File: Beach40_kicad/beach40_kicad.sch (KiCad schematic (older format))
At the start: 75 parts, among them K1 RELAY_2RT, P1 LO In, P2 Mic In, P3 Audio Out, P4 ANT, Q1 BC548, Q2 2N2222, Q3 BD139, Q4 BD139, U1 LM386

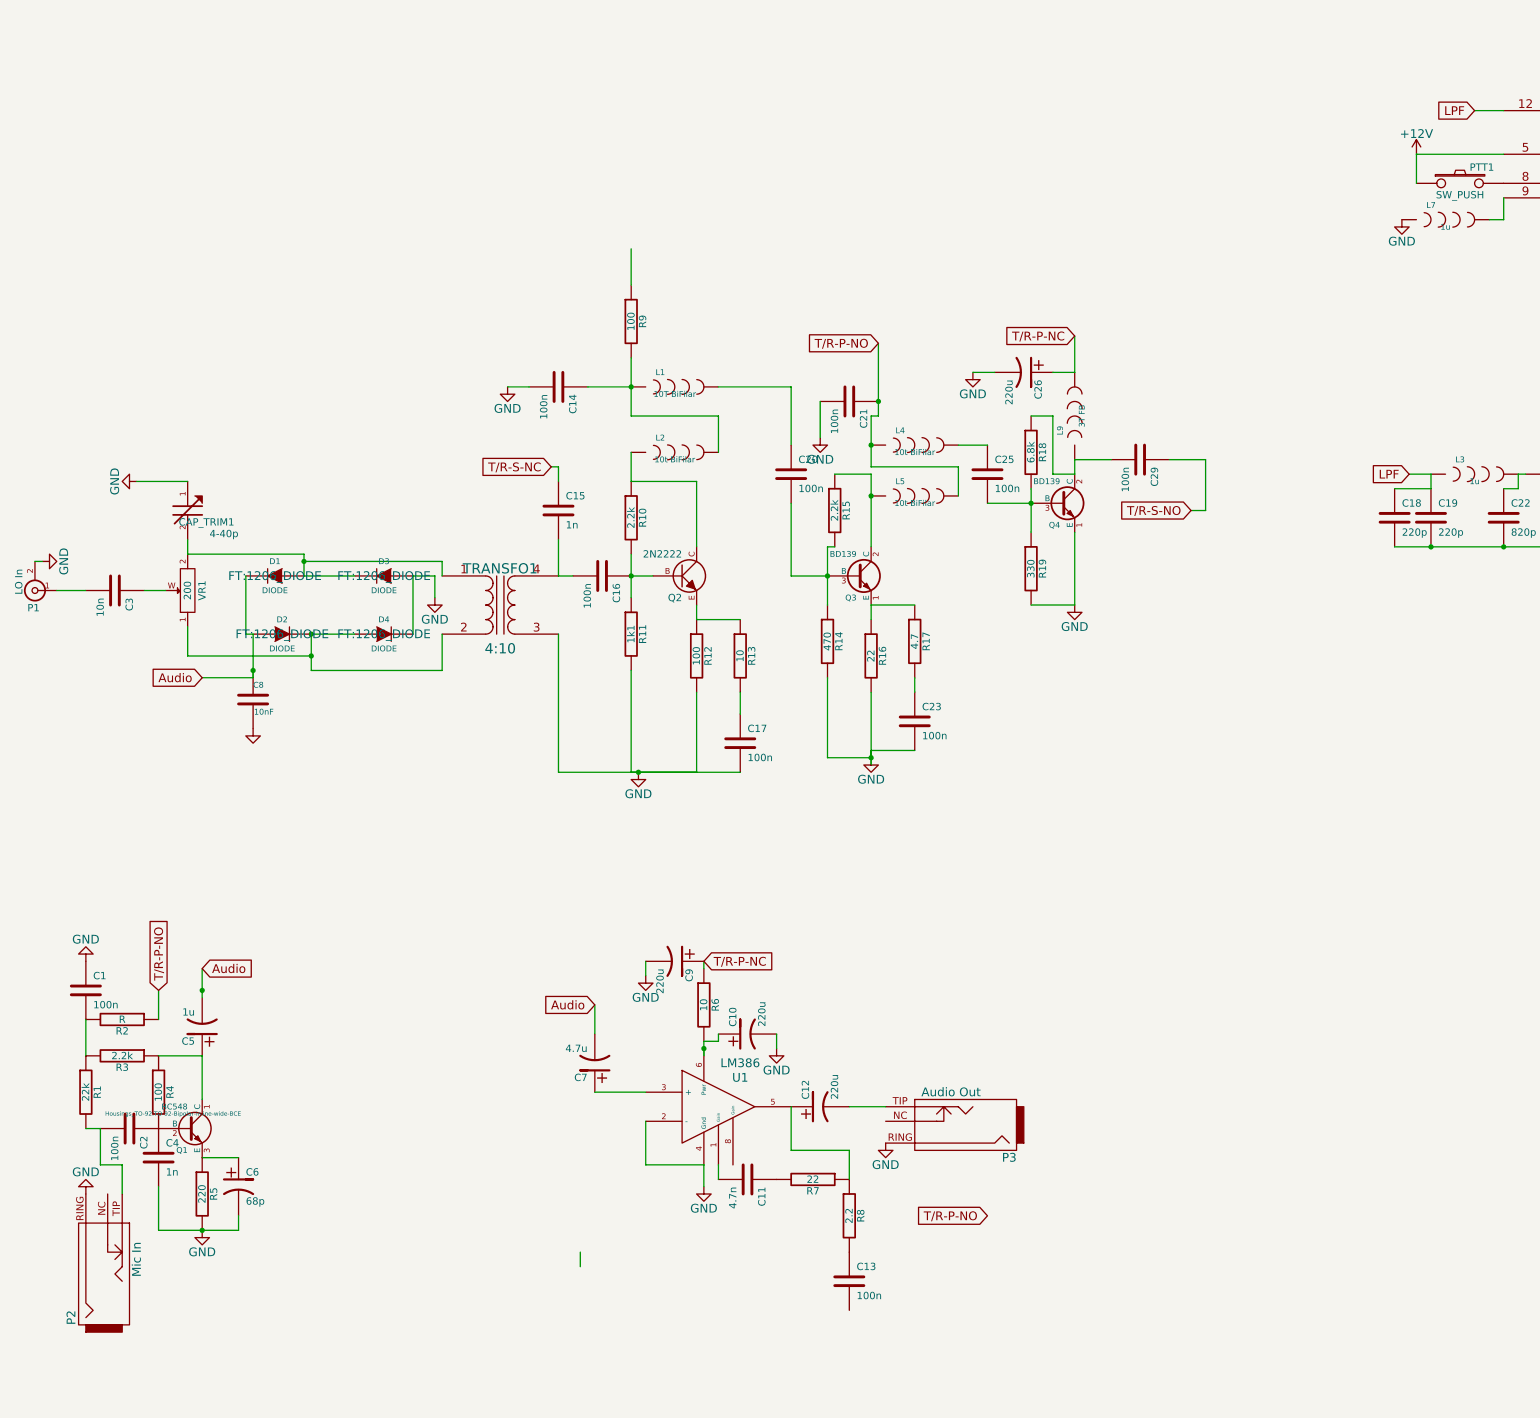
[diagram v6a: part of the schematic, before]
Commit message: Updated schematic to include shunt RC on LM386, Minor changes for ERC, still not quite right, damn gnds and +12v don't want to join the nets.
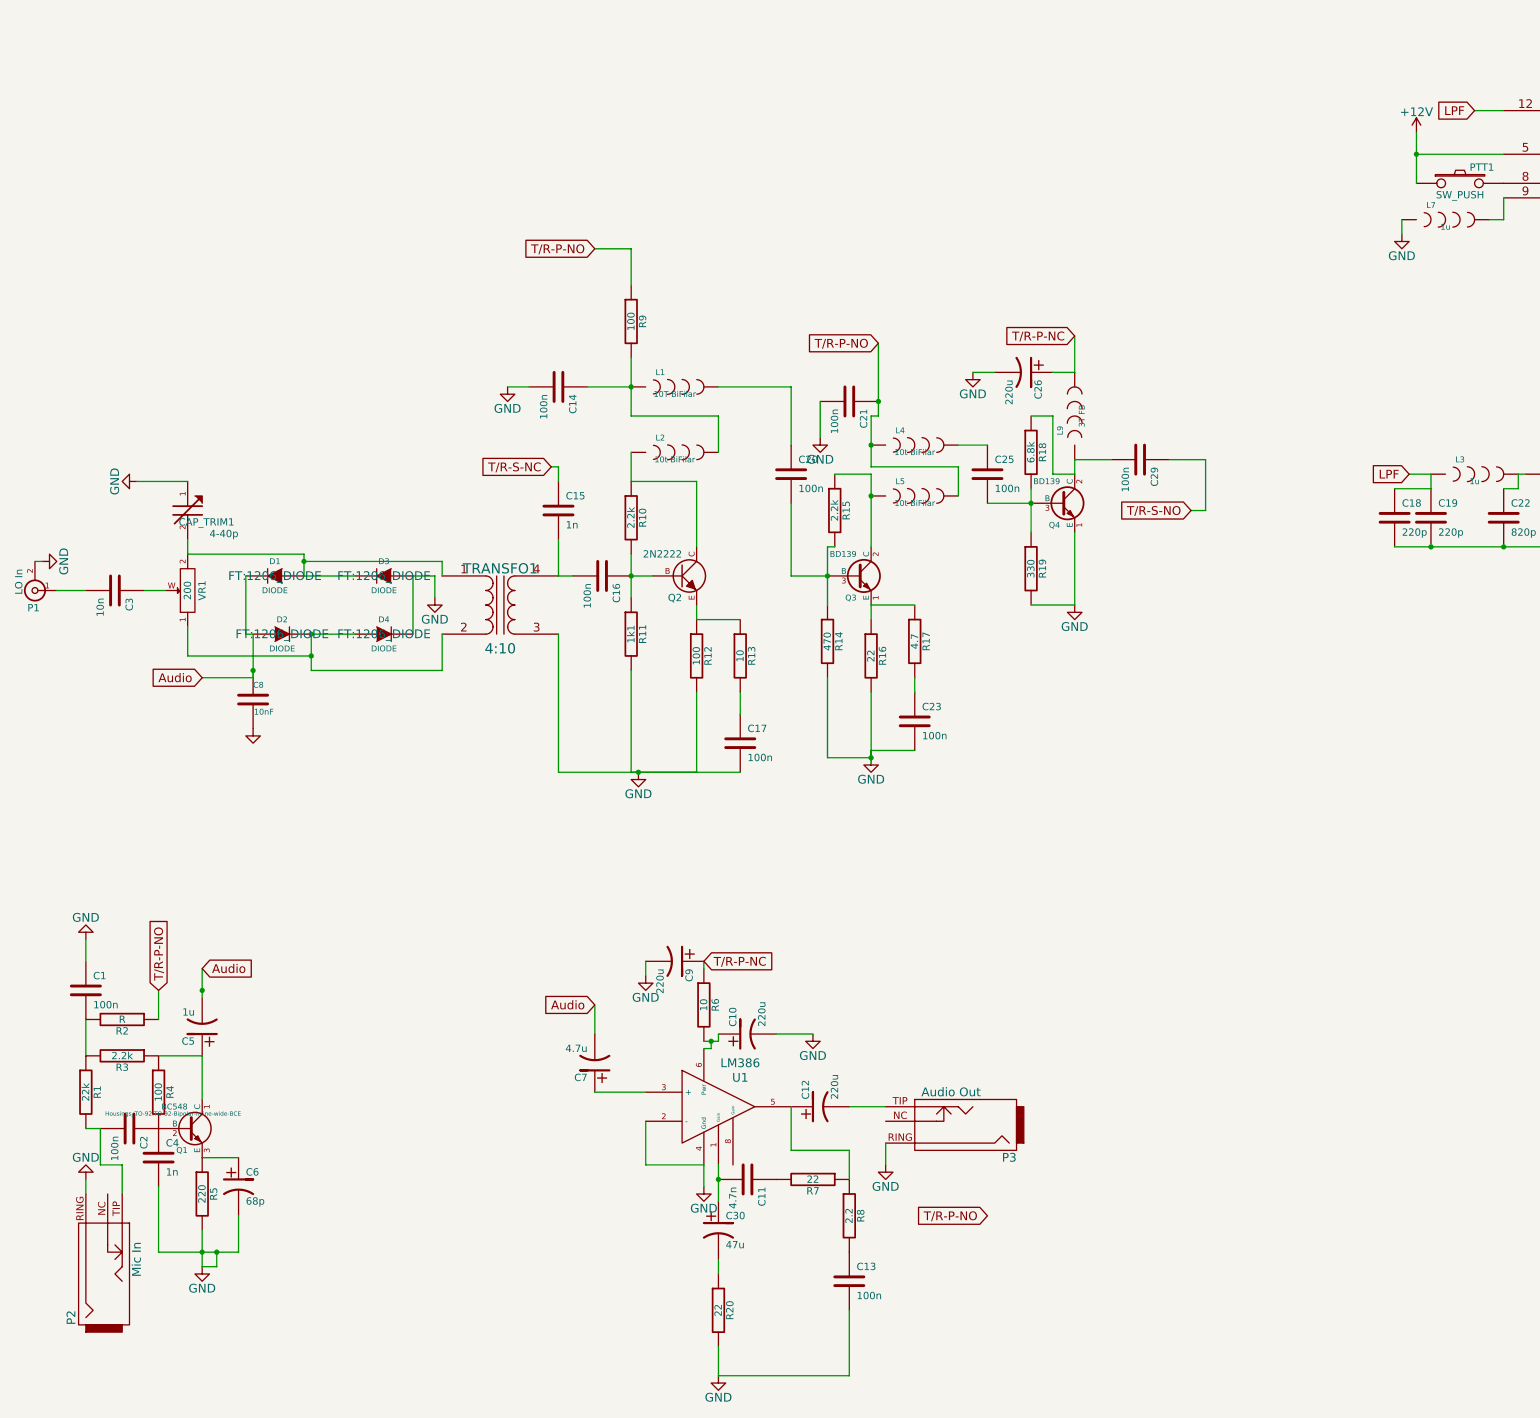
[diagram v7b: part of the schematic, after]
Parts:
- added C30: 47u, Capacitors_ThroughHole:Capacitor3MMDiscRM2.5, symbol C_POL
- added R20: 22, FT:RES_AXIAL_400MIL, symbol R
- U1: footprint (none) -> Housings_SOIC:SOIC-8-1EP_3.9x4.9mm_Pitch1.27mm
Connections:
- wire segments 139 -> 151
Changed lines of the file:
@@
 Wire Wire Line
 	5150 3600 5000 3600
-Wire Wire Line
-	5850 2650 5850 2900
 $Comp
 L CAP C20
@@
 Wire Wire Line
 	12650 1950 13050 1950
-Wire Wire Line
-	11250 2000 11850 2000
 Text GLabel 8300 9300 0    60   Input ~ 0
 T/R-P-NO
@@
 L GND #PWR013
 U 1 1 54D18B38
-P 11150 2450
-F 0 "#PWR013" H 11150 2200 60  0001 C CNN
-F 1 "GND" H 11150 2300 60  0000 C CNN
-F 2 "" H 11150 2450 60  0000 C CNN
-F 3 "" H 11150 2450 60  0000 C CNN
-	1    11150 2450
+P 11150 2550
+F 0 "#PWR013" H 11150 2300 60  0001 C CNN
+F 1 "GND" H 11150 2400 60  0000 C CNN
+F 2 "" H 11150 2550 60  0000 C CNN
+F 3 "" H 11150 2550 60  0000 C CNN
+	1    11150 2550
 	1    0    0    -1
 $EndComp
@@
 F 0 "U1" H 6600 8750 60  0000 C CNN
 F 1 "LM386" H 6600 8850 60  0000 C CNN
-F 2 "" H 6450 8550 60  0001 C CNN
+F 2 "Housings_SOIC:SOIC-8-1EP_3.9x4.9mm_Pitch1.27mm" H 6450 8550 60  0001 C CNN
 F 3 "" H 6450 8550 60  0000 C CNN
 	1    6450 8550
@@
 $EndComp
 Wire Wire Line
-	6450 8950 6450 9050
+	6450 8950 6450 9200
 Wire Wire Line
 	6950 8550 6950 8850
@@
 	7350 8550 7600 8550
 $Comp
-L GND #PWR015
-U 1 1 54D1DADD
-P 7600 8800
-F 0 "#PWR015" H 7600 8550 60  0001 C CNN
-F 1 "GND" H 7600 8650 60  0000 C CNN
-F 2 "" H 7600 8800 60  0000 C CNN
-F 3 "" H 7600 8800 60  0000 C CNN
-	1    7600 8800
-	1    0    0    -1
-$EndComp
-$Comp
 L C_POL C5
 U 1 1 54D1E44B
@@
 	2200 8700 2100 8700
 $Comp
+L GND #PWR015
+U 1 1 54D1FA3E
+P 2100 9050
+F 0 "#PWR015" H 2100 8800 60  0001 C CNN
+F 1 "GND" H 2100 8900 60  0000 C CNN
+F 2 "" H 2100 9050 60  0000 C CNN
+F 3 "" H 2100 9050 60  0000 C CNN
+	1    2100 9050
+	-1   0    0    1
+$EndComp
+$Comp
 L GND #PWR016
-U 1 1 54D1FA3E
-P 2100 9150
-F 0 "#PWR016" H 2100 8900 60  0001 C CNN
-F 1 "GND" H 2100 9000 60  0000 C CNN
-F 2 "" H 2100 9150 60  0000 C CNN
-F 3 "" H 2100 9150 60  0000 C CNN
-	1    2100 9150
-	-1   0    0    1
-$EndComp
-$Comp
-L GND #PWR017
 U 1 1 54D1FA52
-P 2900 9400
-F 0 "#PWR017" H 2900 9150 60  0001 C CNN
-F 1 "GND" H 2900 9250 60  0000 C CNN
-F 2 "" H 2900 9400 60  0000 C CNN
-F 3 "" H 2900 9400 60  0000 C CNN
-	1    2900 9400
+P 2900 9650
+F 0 "#PWR016" H 2900 9400 60  0001 C CNN
+F 1 "GND" H 2900 9500 60  0000 C CNN
+F 2 "" H 2900 9650 60  0000 C CNN
+F 3 "" H 2900 9650 60  0000 C CNN
+	1    2900 9650
 	1    0    0    -1
 $EndComp
@@
 	2900 8900 3150 8900
 Wire Wire Line
-	5500 9650 5500 9550
-Wire Wire Line
-	2600 9400 3150 9400
-Wire Wire Line
-	2600 9100 2600 9400
-Connection ~ 2900 9400
+	2600 9100 2600 9550
 $Comp
 L CAP C1
@@
 	2100 7950 2100 8200
 $Comp
-L GND #PWR018
+L GND #PWR017
 U 1 1 54D225C9
-P 2100 7550
-F 0 "#PWR018" H 2100 7300 60  0001 C CNN
-F 1 "GND" H 2100 7400 60  0000 C CNN
-F 2 "" H 2100 7550 60  0000 C CNN
-F 3 "" H 2100 7550 60  0000 C CNN
-	1    2100 7550
+P 2100 7400
+F 0 "#PWR017" H 2100 7150 60  0001 C CNN
+F 1 "GND" H 2100 7250 60  0000 C CNN
+F 2 "" H 2100 7400 60  0000 C CNN
+F 3 "" H 2100 7400 60  0000 C CNN
+	1    2100 7400
 	-1   0    0    1
 $EndComp
@@
 	2600 7750 2600 7950
 $Comp
-L +12V #PWR019
+L +12V #PWR018
 U 1 1 54D25D14
-P 11250 2000
-F 0 "#PWR019" H 11250 1850 60  0001 C CNN
-F 1 "+12V" H 11250 2140 60  0000 C CNN
-F 2 "" H 11250 2000 60  0000 C CNN
-F 3 "" H 11250 2000 60  0000 C CNN
-	1    11250 2000
-	1    0    0    -1
-$EndComp
-Wire Wire Line
-	11250 2200 11250 2000
+P 11250 1850
+F 0 "#PWR018" H 11250 1700 60  0001 C CNN
+F 1 "+12V" H 11250 1990 60  0000 C CNN
+F 2 "" H 11250 1850 60  0000 C CNN
+F 3 "" H 11250 1850 60  0000 C CNN
+	1    11250 1850
+	1    0    0    -1
+$EndComp
+Wire Wire Line
+	11250 1850 11250 2200
 Wire Wire Line
 	11850 4300 11950 4300
@@
 	13250 4250 13250 4200
 $Comp
-L GND #PWR020
+L GND #PWR019
 U 1 1 54D2CCE0
 P 5950 7650
-F 0 "#PWR020" H 5950 7400 60  0001 C CNN
+F 0 "#PWR019" H 5950 7400 60  0001 C CNN
 F 1 "GND" H 5950 7500 60  0000 C CNN
 F 2 "" H 5950 7650 60  0000 C CNN
@@
 Wire Wire Line
 	5950 7550 5950 7650
-$Comp
-L GND #PWR021
-U 1 1 54D2D156
-P 6850 8150
-F 0 "#PWR021" H 6850 7900 60  0001 C CNN
-F 1 "GND" H 6850 8000 60  0000 C CNN
-F 2 "" H 6850 8150 60  0000 C CNN
-F 3 "" H 6850 8150 60  0000 C CNN
-	1    6850 8150
-	1    0    0    -1
-$EndComp
-Wire Wire Line
-	6850 8050 6850 8150
 $Comp
 L R R6
@@
 	6350 7550 6350 7600
 Wire Wire Line
-	6350 8100 6350 8200
-Connection ~ 6350 8150
-Wire Wire Line
 	6350 8100 6450 8100
 Wire Wire Line
@@
 Audio
 Wire Wire Line
-	3150 9400 3150 9300
+	3150 9550 3150 9300
+$Comp
+L C_POL C30
+U 1 1 54EFD057
+P 6450 9400
+F 0 "C30" H 6500 9500 50  0000 L CNN
+F 1 "47u" H 6500 9300 50  0000 L CNN
+F 2 "Capacitors_ThroughHole:Capacitor3MMDiscRM2.5" H 6450 9400 60  0001 C CNN
+F 3 "" H 6450 9400 60  0000 C CNN
+	1    6450 9400
+	1    0    0    -1
+$EndComp
+$Comp
+L R R20
+U 1 1 54EFD084
+P 6450 9950
+F 0 "R20" V 6530 9950 50  0000 C CNN
+F 1 "22" V 6450 9950 50  0000 C CNN
+F 2 "FT:RES_AXIAL_400MIL" H 6450 9950 60  0001 C CNN
+F 3 "" H 6450 9950 60  0000 C CNN
+	1    6450 9950
+	1    0    0    -1
+$EndComp
+Wire Wire Line
+	6450 9700 6450 9600
+Connection ~ 6450 9050
+$Comp
+L GND #PWR020
+U 1 1 54EFD734
+P 6450 10400
+F 0 "#PWR020" H 6450 10150 60  0001 C CNN
+F 1 "GND" H 6450 10250 60  0000 C CNN
+F 2 "" H 6450 10400 60  0000 C CNN
+F 3 "" H 6450 10400 60  0000 C CNN
+	1    6450 10400
+	1    0    0    -1
+$EndComp
+Wire Wire Line
+	6450 10400 6450 10200
+Wire Wire Line
+	7350 9950 7350 10400
+Wire Wire Line
+	7350 10400 6450 10400
+Wire Wire Line
+	6350 8150 6400 8150
+Wire Wire Line
+	6400 8150 6400 8100
+Connection ~ 6400 8100
+$Comp
+L GND #PWR021
+U 1 1 54EFF3FC
+P 7100 8050
+F 0 "#PWR021" H 7100 7800 60  0001 C CNN
+F 1 "GND" H 7100 7900 60  0000 C CNN
+F 2 "" H 7100 8050 60  0000 C CNN
+F 3 "" H 7100 8050 60  0000 C CNN
+	1    7100 8050
+	1    0    0    -1
+$EndComp
+Wire Wire Line
+	6850 8050 7100 8050
+$Comp
+L GND #PWR022
+U 1 1 54EFF911
+P 7600 8950
+F 0 "#PWR022" H 7600 8700 60  0001 C CNN
+F 1 "GND" H 7600 8800 60  0000 C CNN
+F 2 "" H 7600 8950 60  0000 C CNN
+F 3 "" H 7600 8950 60  0000 C CNN
+	1    7600 8950
+	1    0    0    -1
+$EndComp
+Wire Wire Line
+	7600 8800 7600 8950
+Connection ~ 11250 2000
+Wire Wire Line
+	2100 9150 2100 9050
+Wire Wire Line
+	11150 2450 11150 2550
+Wire Wire Line
+	11250 2000 11850 2000
+Wire Wire Line
+	2100 7550 2100 7400
+Text GLabel 5600 2650 0    60   Input ~ 0
+T/R-P-NO
+Wire Wire Line
+	5600 2650 5850 2650
+Wire Wire Line
+	5850 2650 5850 2900
+Wire Wire Line
+	2900 9400 2900 9650
+Wire Wire Line
+	2600 9550 3150 9550
+Connection ~ 2900 9550
+Wire Wire Line
+	2900 9650 3000 9650
+Wire Wire Line
+	3000 9650 3000 9550
+Connection ~ 3000 9550
 $EndSCHEMATC

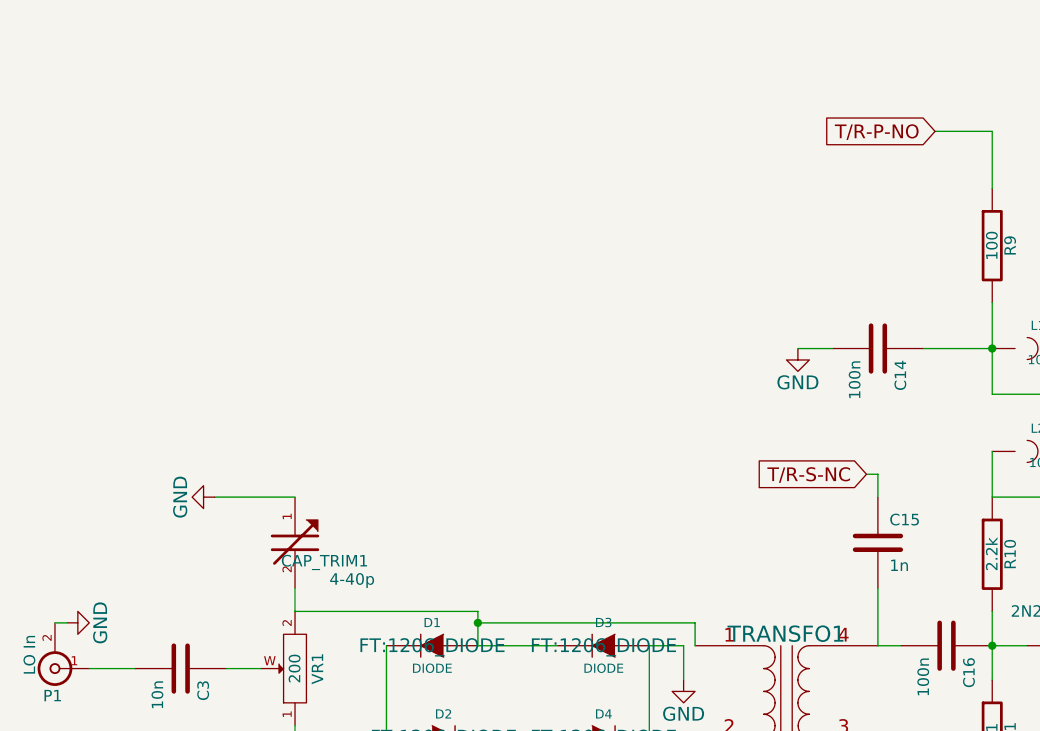
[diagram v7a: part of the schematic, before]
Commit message: - updates for RX pre-amp
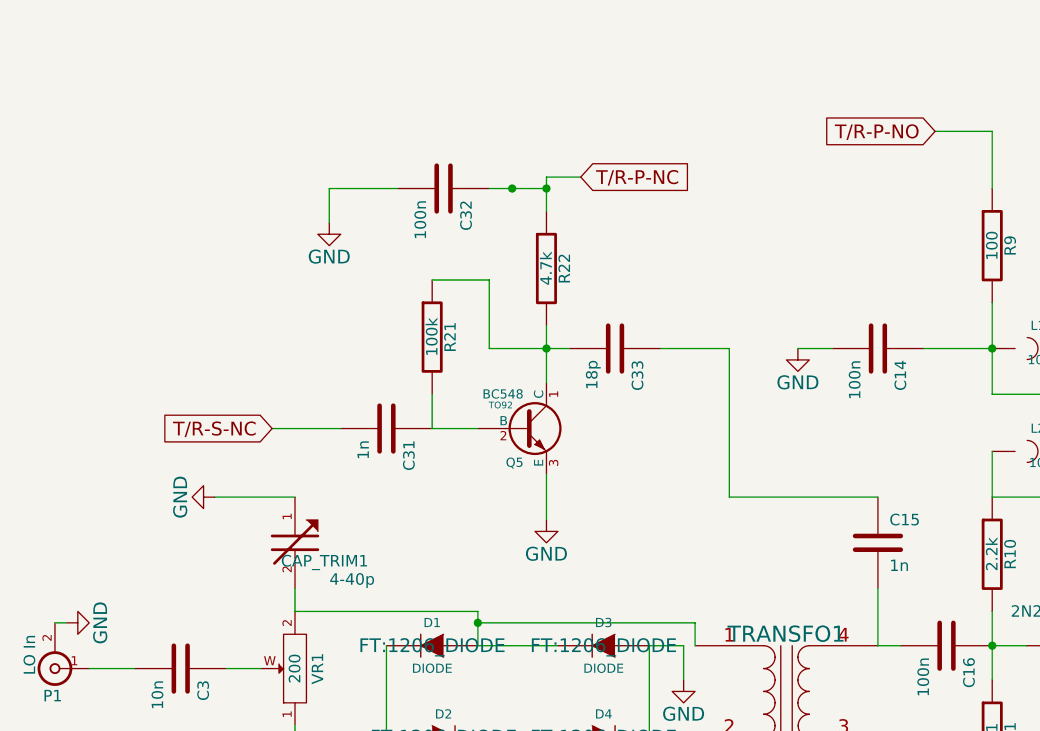
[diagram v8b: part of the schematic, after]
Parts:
- added C31: 1n, symbol CAP
- added C32: 100n, symbol CAP
- added C33: 18p, symbol CAP
- added Q5: BC548, TO92, symbol BC548
- added R21: 100k, symbol R
- added R22: 4.7k, symbol R
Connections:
- net GND: now also C32.2, Q5.3 (E)
- net T/R-P-NC: now also C32.1, R22.1
- net T/R-S-NC: now also C31.2; no longer C15.1
- new net: C15.1, C33.1
- new net: C33.2, Q5.1 (C), R21.1, R22.2
- new net: C31.1, Q5.2 (B), R21.2
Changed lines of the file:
@@
 Wire Wire Line
 	5350 4900 5450 4900
-Text GLabel 5300 4150 0    60   Input ~ 0
+Text GLabel 2700 3950 0    60   Input ~ 0
 T/R-S-NC
 $Comp
@@
 	1    0    0    -1
 $EndComp
-Wire Wire Line
-	5350 4250 5350 4150
-Wire Wire Line
-	5350 4150 5300 4150
 $Comp
 L CAP C3
@@
 	3000 9650 3000 9550
 Connection ~ 3000 9550
+$Comp
+L R R22
+U 1 1 54F55C0A
+P 3900 3250
+F 0 "R22" V 3980 3250 50  0000 C CNN
+F 1 "4.7k" V 3900 3250 50  0000 C CNN
+F 2 "" H 3900 3250 60  0000 C CNN
+F 3 "" H 3900 3250 60  0000 C CNN
+	1    3900 3250
+	1    0    0    -1
+$EndComp
+$Comp
+L R R21
+U 1 1 54F55C59
+P 3400 3550
+F 0 "R21" V 3480 3550 50  0000 C CNN
+F 1 "100k" V 3400 3550 50  0000 C CNN
+F 2 "" H 3400 3550 60  0000 C CNN
+F 3 "" H 3400 3550 60  0000 C CNN
+	1    3400 3550
+	1    0    0    -1
+$EndComp
+$Comp
+L CAP C31
+U 1 1 54F55C84
+P 3200 3950
+F 0 "C31" H 3250 4050 50  0000 L CNN
+F 1 "1n" H 3250 3850 50  0000 L CNN
+F 2 "" H 3200 3950 60  0000 C CNN
+F 3 "" H 3200 3950 60  0000 C CNN
+	1    3200 3950
+	0    1    1    0
+$EndComp
+$Comp
+L CAP C33
+U 1 1 54F55CAF
+P 4200 3600
+F 0 "C33" H 4250 3700 50  0000 L CNN
+F 1 "18p" H 4250 3500 50  0000 L CNN
+F 2 "" H 4200 3600 60  0000 C CNN
+F 3 "" H 4200 3600 60  0000 C CNN
+	1    4200 3600
+	0    1    1    0
+$EndComp
+$Comp
+L CAP C32
+U 1 1 54F55CEA
+P 3450 2900
+F 0 "C32" H 3500 3000 50  0000 L CNN
+F 1 "100n" H 3500 2800 50  0000 L CNN
+F 2 "" H 3450 2900 60  0000 C CNN
+F 3 "" H 3450 2900 60  0000 C CNN
+	1    3450 2900
+	0    1    1    0
+$EndComp
+$Comp
+L BC548 Q5
+U 1 1 54F55D21
+P 3800 3950
+F 0 "Q5" H 3800 3801 40  0000 R CNN
+F 1 "BC548" H 3800 4100 40  0000 R CNN
+F 2 "TO92" H 3700 4052 29  0000 C CNN
+F 3 "" H 3800 3950 60  0000 C CNN
+	1    3800 3950
+	1    0    0    -1
+$EndComp
+Text GLabel 4050 2850 2    60   Input ~ 0
+T/R-P-NC
+Wire Wire Line
+	4050 2850 3900 2850
+Wire Wire Line
+	3900 2850 3900 3000
+Wire Wire Line
+	3650 2900 3900 2900
+Connection ~ 3900 2900
+Wire Wire Line
+	3900 3500 3900 3750
+Wire Wire Line
+	3650 3600 4000 3600
+Connection ~ 3900 3600
+Wire Wire Line
+	3400 3800 3400 3950
+Wire Wire Line
+	3400 3950 3600 3950
+Wire Wire Line
+	3000 3950 2700 3950
+Connection ~ 3750 2900
+Wire Wire Line
+	3400 3300 3650 3300
+Wire Wire Line
+	3650 3300 3650 3600
+Wire Wire Line
+	4400 3600 4700 3600
+Wire Wire Line
+	4700 3600 4700 4250
+Wire Wire Line
+	4700 4250 5350 4250
+$Comp
+L GND #PWR023
+U 1 1 54F5805B
+P 3900 4350
+F 0 "#PWR023" H 3900 4100 60  0001 C CNN
+F 1 "GND" H 3900 4200 60  0000 C CNN
+F 2 "" H 3900 4350 60  0000 C CNN
+F 3 "" H 3900 4350 60  0000 C CNN
+	1    3900 4350
+	1    0    0    -1
+$EndComp
+$Comp
+L GND #PWR024
+U 1 1 54F5806F
+P 2950 3050
+F 0 "#PWR024" H 2950 2800 60  0001 C CNN
+F 1 "GND" H 2950 2900 60  0000 C CNN
+F 2 "" H 2950 3050 60  0000 C CNN
+F 3 "" H 2950 3050 60  0000 C CNN
+	1    2950 3050
+	1    0    0    -1
+$EndComp
+Wire Wire Line
+	3250 2900 2950 2900
+Wire Wire Line
+	2950 2900 2950 3050
+Wire Wire Line
+	3900 4150 3900 4350
 $EndSCHEMATC
